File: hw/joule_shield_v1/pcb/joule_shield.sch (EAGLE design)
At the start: 80 parts, among them J4 USB_AUSB_A_SMT_RA, J5 JST-ZH5JST_ZH_SMT_VERT, J6 INTEL_JOULE_J6, J7 INTEL_JOULE_J7, U1 BQ25892PWQFN-24, U2 FAN8623WLCSP16, U3 TPS63201PVSON-14, U4 TLV62084PWSON-8, U5 TPS2553PWSON-6, U6 TPS2553PWSON-6, U7 SINGLE-BIT_BUS_TRANSCEIVER, U8 SINGLE-BIT_BUS_TRANSCEIVER

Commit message: Schematic for RTC battery.
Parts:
- added D3: ESD_DIODEM1005, joule_shield:ESD_DIODEM1005
- added JRTC: BK-916BK-916, joule_shield:BK-916BK-916
- added R25: 1k, mf_passives:RESISTOR_0603
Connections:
- new net N$30: D3.P$2, JRTC.VBAT, R25.P$1
- new net VRTC: R25.P$2
- net GND: now also D3.P$1, JRTC.GND
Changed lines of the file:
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@@
 <part name="U$33" library="joule_shield" deviceset="V5P0V_USBB" device=""/>
 <part name="GND34" library="supply1" deviceset="GND" device=""/>
+<part name="JRTC" library="joule_shield" deviceset="BK-916" device="BK-916"/>
+<part name="GND35" library="supply1" deviceset="GND" device=""/>
+<part name="R25" library="mf_passives" deviceset="RESISTOR" device="_0603" value="1k">
+<attribute name="MPN" value="MF-RES-0603-1K"/>
+</part>
+<part name="U$37" library="joule_shield" deviceset="VRTC" device=""/>
+<part name="GND36" library="supply1" deviceset="GND" device=""/>
+<part name="D3" library="joule_shield" deviceset="ESD_DIODE" device="M1005">
+<attribute name="DPN" value="490-13209-1-ND"/>
+<attribute name="MPN" value="LXES15AAA1-133"/>
+</part>
 </parts>
 <sheets>
@@
 </segment>
 </net>
+</nets>
+</sheet>
+<sheet>
+<plain>
+</plain>
+<instances>
+<instance part="JRTC" gate="G$1" x="17.78" y="45.72"/>
+<instance part="GND35" gate="1" x="43.18" y="30.48"/>
+<instance part="R25" gate="G$1" x="60.96" y="50.8" rot="R90"/>
+<instance part="U$37" gate="G$1" x="78.74" y="58.42"/>
+<instance part="GND36" gate="1" x="55.88" y="22.86"/>
+<instance part="D3" gate="G$1" x="55.88" y="38.1" rot="R90">
+<attribute name="DPN" x="55.88" y="38.1" size="1.778" layer="96" rot="R90" display="off"/>
+<attribute name="MPN" x="55.88" y="38.1" size="1.778" layer="96" rot="R90" display="off"/>
+</instance>
+</instances>
+<busses>
+</busses>
+<nets>
+<net name="GND" class="0">
+<segment>
+<pinref part="JRTC" gate="G$1" pin="GND"/>
+<wire x1="35.56" y1="38.1" x2="43.18" y2="38.1" width="0.1524" layer="91"/>
+<pinref part="GND35" gate="1" pin="GND"/>
+<wire x1="43.18" y1="38.1" x2="43.18" y2="33.02" width="0.1524" layer="91"/>
+</segment>
+<segment>
+<pinref part="D3" gate="G$1" pin="P$1"/>
+<pinref part="GND36" gate="1" pin="GND"/>
+<wire x1="55.88" y1="27.94" x2="55.88" y2="25.4" width="0.1524" layer="91"/>
+</segment>
+</net>
+<net name="VRTC" class="0">
+<segment>
+<pinref part="R25" gate="G$1" pin="P$2"/>
+<pinref part="U$37" gate="G$1" pin="VRTC"/>
+<wire x1="66.04" y1="50.8" x2="78.74" y2="50.8" width="0.1524" layer="91"/>
+<wire x1="78.74" y1="50.8" x2="78.74" y2="58.42" width="0.1524" layer="91"/>
+</segment>
+</net>
+<net name="N$30" class="0">
+<segment>
+<pinref part="R25" gate="G$1" pin="P$1"/>
+<pinref part="JRTC" gate="G$1" pin="VBAT"/>
+<wire x1="55.88" y1="50.8" x2="35.56" y2="50.8" width="0.1524" layer="91"/>
+<pinref part="D3" gate="G$1" pin="P$2"/>
+<wire x1="55.88" y1="48.26" x2="55.88" y2="50.8" width="0.1524" layer="91"/>
+<junction x="55.88" y="50.8"/>
+</segment>
+</net>

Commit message: Add part numbers for all the major ICs and schematic for SD card.
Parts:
- added C33, C34, C36: 0.1uF, mf_passives:CAPACITOR_NP_0603
- added C35: 10uF, mf_passives:CAPACITOR_NP_0603
- added FB1, FB2: FERRITE_BEAD, joule_shield:FERRITE_BEAD
- added R26: 100k, mf_passives:RESISTOR_0603
- added U$40: DM3ATDM3AT, joule_shield:DM3ATDM3AT
- added U9: TXS0206-29, joule_shield:TXS0206-29
- J6, J7: DPN (none) -> H11615CT-ND; MF (none) -> Hirose Electric Co Ltd; MPN (none) -> DF40C-100DS-0.4V(51)
- JD1, JD2: DPN (none) -> 455-2262-1-ND; MF (none) -> JST Sales America Inc.; MPN (none) -> S4B-XH-SM4-TB(LF)(SN)
- JRTC: DPN (none) -> BK-916-CT-ND; MF (none) -> MPD (Memory Protection Devices); MPN (none) -> BK-916-TR
- U1: DPN (none) -> 296-41131-1-ND; MF (none) -> Texas Instruments; MPN (none) -> BQ25892RTWT
- U3: DPN (none) -> 296-27259-1-ND; MF (none) -> Texas Instruments; MPN (none) -> TPS63021DSJR
- U4: MF (none) -> Texas Instruments; MOUSER (none) -> 595-TLV62084DSGR; MPN (none) -> TLV62084DSGR
- U5, U6: DPN (none) -> 296-23999-1-ND; MF (none) -> Texas Instruments; MPN (none) -> TPS2553DRVT
- U7, U8: DPN (none) -> 296-16843-1-ND; MF (none) -> Texas Instruments; MPN (none) -> SN74LVC1T45DBVR
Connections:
- new net N$35: C36.P$1, U$40.VDD, U9.VCCB
- new net N$37: C34.P$1, C35.P$1, FB2.P$1, U9.VBATT
- new net N$38: C33.P$1, FB1.P$2, U9.VCCA
- new net N$40: U$40.DAT0, U9.DAT0B
- new net N$41: U$40.DAT1, U9.DAT1B
- new net N$42: U$40.DAT2, U9.DAT2B
- new net N$43: U$40.CD/DAT3, U9.DAT3B
- new net N$44: U$40.CMD, U9.CMDB
- new net N$45: U$40.CLK, U9.CLKB
- new net SDCARD_CD: J6.SDCARD_CD_N, U$40.CDA, U9.WP/CD
- new net SDCARD_CLK: J6.SDCARD_CLK, U9.CLKA
- new net SDCARD_CLK_FB: J6.SDCARD_LVL_CLK_FB, U9.CLK-F
- new net SDCARD_CMD: J6.SDCARD_CMD, U9.CMDA
- new net SDCARD_D0: J6.SDCARD_D0, U9.DAT0A
- new net SDCARD_D1: J6.SDCARD_D1, U9.DAT1A
- new net SDCARD_D2: J6.SDCARD_D2, U9.DAT2A
- new net SDCARD_D3: J6.SDCARD_D3, U9.DAT3A
- new net SDCARD_PWR_DOWN_N: J6.SDCARD_PWR_DOWN_N, R26.P$1, U9.EN
- net GND: now also C33.P$2, C34.P$2, C35.P$2, C36.P$2, R26.P$2, U$40.CDB, U$40.GND, U$40.VSS, U9.GND
- net V1P8V: now also FB1.P$1
- net V3P3V: now also FB2.P$2

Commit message: Schematic for Fan, BIOS USB-serial, and LEDs.
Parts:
- added C37, C38, C39, C40: 0.1uF, mf_passives:CAPACITOR_NP_0603
- added D10, D11: MF-LED-0603-GREEN, mf_leds:LED_SINGLE-0603-GREEN
- added D4, D5, D6, D7: ESD_DIODEM1005, joule_shield:ESD_DIODEM1005
- added D8, D9: MF-LED-0603-RED, mf_leds:LED_SINGLE-0603-RED
- added FB3: FERRITE_BEAD, joule_shield:FERRITE_BEAD
- added J1: MF-CON-MICROUSB-RIGHT, mf_connectors:USB_MICRO_RIGHT
- added R27: 10k, mf_passives:RESISTOR_0603
- added R28, R29: 27, mf_passives:RESISTOR_0603
- added R30: 0, mf_passives:RESISTOR_0603
- added R31: 100, mf_passives:RESISTOR_0603
- added R32: 100k, mf_passives:RESISTOR_0603
- added R33, R34, R35, R36: 1k, mf_passives:RESISTOR_0603
- added R37, R38, R39, R40: 470, mf_passives:RESISTOR_0603
- added SW1, SW2, SW3: MF-SW-TACT-6MM, mf_switches:TACT_6MM
- added U$41: AMP_MINI_FAN, joule_shield:AMP_MINI_FAN
- added U10: FT231XQFN-20, joule_shield:FT231XQFN-20
- added U11, U12, U13, U14: MF-DSC-SOT233-MMBT3904, mf_discrete_semiconductor:NPN_BJTMMBT3904_SOT-23-3
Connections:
- new net BTN_N: D7.P$2, J6.GPIO_17, SW3.P$2
- new net ISH_GPIO_0: J6.ISH_GPIO_0, R33.P$1
- new net ISH_GPIO_1: J6.ISH_GPIO_1, R34.P$1
- new net ISH_GPIO_2: J6.ISH_GPIO_2, R35.P$1
- new net ISH_GPIO_3: J6.ISH_GPIO_3, R36.P$1
- new net N$36: R27.P$2, U$41.2
- new net N$39: R28.P$2, U10.USBDM
- new net N$46: D4.P$2, FB3.P$1, J1.5V
- new net N$47: R29.P$2, U10.USBDP
- new net N$48: J1.D+, R29.P$1
- new net N$49: C38.P$1, FB3.P$2, U10.VCC
- new net N$50: J1.D-, R28.P$1
- new net N$51: R30.P$2, U1./QON
- new net N$52: R31.P$2, SW2.P$3
- new net N$53: C40.P$1, U10.3V3OUT
- new net N$54: R32.P$2, SW3.P$1
- new net N$55: D11.ANODE, R40.P$2
- new net N$56: D10.ANODE, R39.P$2
- new net N$57: D9.ANODE, R38.P$2
- new net N$58: D8.ANODE, R37.P$2
- new net N$59: D8.CATHODE, U11.COLLECTOR
- new net N$60: D9.CATHODE, U12.COLLECTOR
- new net N$61: D10.CATHODE, U13.COLLECTOR
- new net N$62: D11.CATHODE, U14.COLLECTOR
- new net N$63: R33.P$2, U11.BASE
- new net N$64: R34.P$2, U12.BASE
- new net N$65: R35.P$2, U13.BASE
- new net N$66: R36.P$2, U14.BASE
- new net PMIC_PWRBTN_N: D5.P$2, R30.P$1, SW1.P$2
- new net UART2_CTS: J6.UART2_CTS, U10.RTS/
- new net UART2_RTS: J6.UART2_RTS, U10.CTS/
- new net UART2_RX: J6.UART2_RXD, U10.TXD
- new net UART2_TX: D6.P$2, J6.UART2_TXD, SW2.P$2, U10.RXD
- net GND: now also C37.P$2, C38.P$2, C39.P$2, C40.P$2, D4.P$1, D5.P$1, D6.P$1, D7.P$1, J1.GND, J1.SLD, SW1.P$3, SW3.P$3, U$41.3, U$41.SHLD, U10.AGND, U10.GND, U11.EMITTER, U12.EMITTER, U13.EMITTER, U14.EMITTER
- net V1P8V: now also C39.P$1, U10.VCCIO
- net V3P3V: now also R27.P$1
- net V5P0V: now also C37.P$1, R37.P$1, R38.P$1, R39.P$1, R40.P$1, U$41.1
- net VDD1: now also R31.P$1, R32.P$1
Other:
- note added: "Boot from DNX"
- note added: "Power Button"

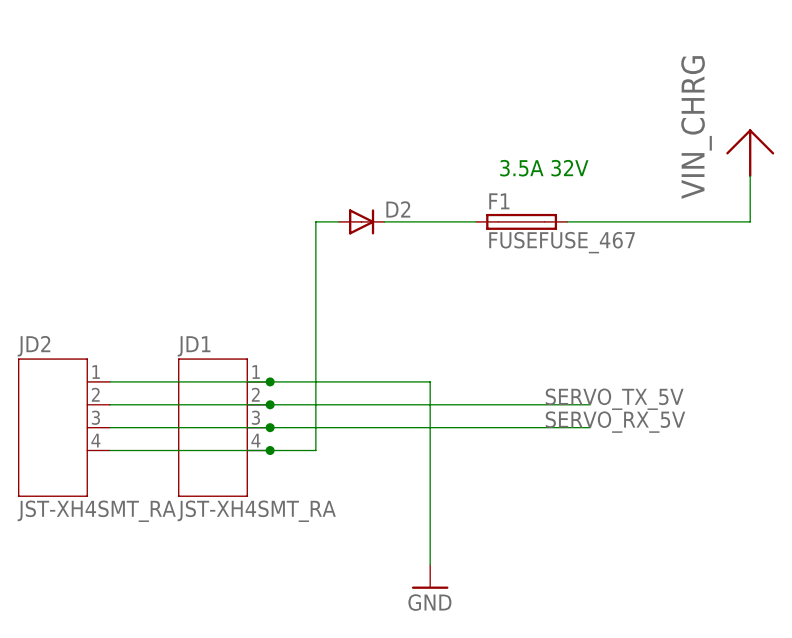
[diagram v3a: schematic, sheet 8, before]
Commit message: joule shield: Begin rough layout.
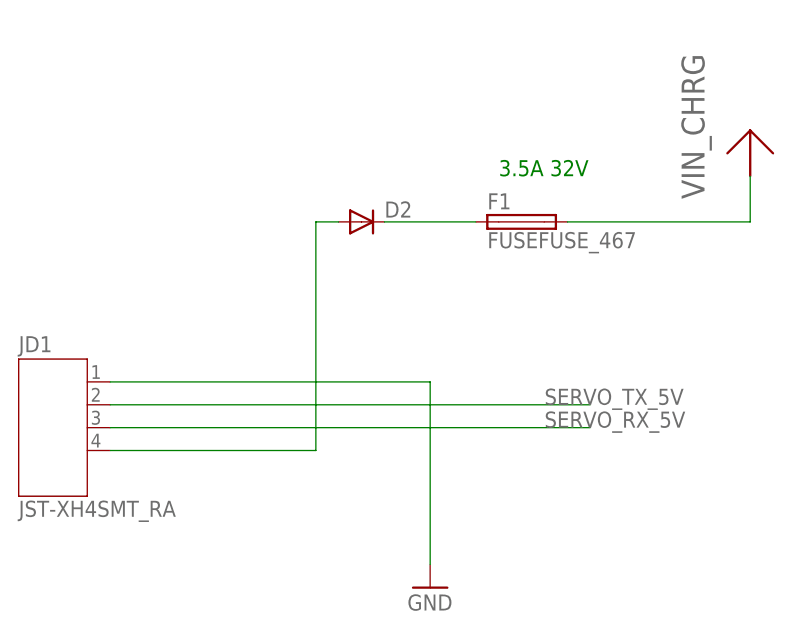
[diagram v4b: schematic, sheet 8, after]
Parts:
- removed JD2: JST-XH4SMT_RA, joule_shield:JST-XH4SMT_RA
- added U$48, U$49, U$50, U$51: SMTSOSMTSO-M1.6, joule_shield:SMTSOSMTSO-M1.6
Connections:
- net GND: no longer JD2.1
- net N$28: no longer JD2.4
- net SERVO_RX_5V: no longer JD2.3
- net SERVO_TX_5V: no longer JD2.2
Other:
- moved on the sheet: JD1
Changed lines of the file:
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@@
 </part>
 <part name="U$26" library="joule_shield" deviceset="V1P8V" device=""/>
-<part name="JD1" library="joule_shield" deviceset="JST-XH4" device="SMT_RA">
-<attribute name="DPN" value="455-2262-1-ND"/>
-<attribute name="MF" value="JST Sales America Inc."/>
-<attribute name="MPN" value="S4B-XH-SM4-TB(LF)(SN)"/>
-</part>
 <part name="GND26" library="supply1" deviceset="GND" device=""/>
 <part name="U$28" library="joule_shield" deviceset="VIN_CHRG" device=""/>
-<part name="JD2" library="joule_shield" deviceset="JST-XH4" device="SMT_RA">
+<part name="JD1" library="joule_shield" deviceset="JST-XH4" device="SMT_RA">
 <attribute name="DPN" value="455-2262-1-ND"/>
 <attribute name="MF" value="JST Sales America Inc."/>
@@
 </part>
 <part name="U$47" library="joule_shield" deviceset="V5P0V" device=""/>
+<part name="U$48" library="joule_shield" deviceset="SMTSO" device="SMTSO-M1.6"/>
+<part name="U$49" library="joule_shield" deviceset="SMTSO" device="SMTSO-M1.6"/>
+<part name="U$50" library="joule_shield" deviceset="SMTSO" device="SMTSO-M1.6"/>
+<part name="U$51" library="joule_shield" deviceset="SMTSO" device="SMTSO-M1.6"/>
 </parts>
 <sheets>
@@
 <instance part="U$33" gate="G$1" x="279.4" y="93.98"/>
 <instance part="GND34" gate="1" x="287.02" y="60.96"/>
+<instance part="U$48" gate="G$1" x="-25.4" y="-22.86"/>
+<instance part="U$49" gate="G$1" x="-7.62" y="-22.86"/>
+<instance part="U$50" gate="G$1" x="10.16" y="-22.86"/>
+<instance part="U$51" gate="G$1" x="27.94" y="-22.86"/>
 </instances>
 <busses>
@@
 </plain>
 <instances>
-<instance part="JD1" gate="G$1" x="35.56" y="83.82">
-<attribute name="DPN" x="35.56" y="83.82" size="1.778" layer="96" display="off"/>
-<attribute name="MF" x="35.56" y="83.82" size="1.778" layer="96" display="off"/>
-<attribute name="MPN" x="35.56" y="83.82" size="1.778" layer="96" display="off"/>
-</instance>
 <instance part="GND26" gate="1" x="60.96" y="66.04"/>
 <instance part="U$28" gate="G$1" x="96.52" y="111.76"/>
-<instance part="JD2" gate="G$1" x="17.78" y="83.82">
+<instance part="JD1" gate="G$1" x="17.78" y="83.82">
 <attribute name="DPN" x="17.78" y="83.82" size="1.778" layer="96" display="off"/>
 <attribute name="MF" x="17.78" y="83.82" size="1.778" layer="96" display="off"/>
@@
 <wire x1="60.96" y1="68.58" x2="60.96" y2="88.9" width="0.1524" layer="91"/>
 <pinref part="JD1" gate="G$1" pin="1"/>
-<wire x1="60.96" y1="88.9" x2="43.18" y2="88.9" width="0.1524" layer="91"/>
-<pinref part="JD2" gate="G$1" pin="1"/>
-<wire x1="25.4" y1="88.9" x2="43.18" y2="88.9" width="0.1524" layer="91"/>
-<junction x="43.18" y="88.9"/>
+<wire x1="25.4" y1="88.9" x2="60.96" y2="88.9" width="0.1524" layer="91"/>
 </segment>
 </net>
 <net name="SERVO_TX_5V" class="0">
 <segment>
+<wire x1="25.4" y1="86.36" x2="78.74" y2="86.36" width="0.1524" layer="91"/>
+<label x="73.66" y="86.36" size="1.778" layer="95"/>
 <pinref part="JD1" gate="G$1" pin="2"/>
-<wire x1="43.18" y1="86.36" x2="78.74" y2="86.36" width="0.1524" layer="91"/>
-<label x="73.66" y="86.36" size="1.778" layer="95"/>
-<pinref part="JD2" gate="G$1" pin="2"/>
-<wire x1="43.18" y1="86.36" x2="25.4" y2="86.36" width="0.1524" layer="91"/>
-<junction x="43.18" y="86.36"/>
 </segment>
 </net>
 <net name="SERVO_RX_5V" class="0">
 <segment>
+<wire x1="25.4" y1="83.82" x2="78.74" y2="83.82" width="0.1524" layer="91"/>
+<label x="73.66" y="83.82" size="1.778" layer="95"/>
 <pinref part="JD1" gate="G$1" pin="3"/>
-<wire x1="43.18" y1="83.82" x2="78.74" y2="83.82" width="0.1524" layer="91"/>
-<label x="73.66" y="83.82" size="1.778" layer="95"/>
-<pinref part="JD2" gate="G$1" pin="3"/>
-<wire x1="25.4" y1="83.82" x2="43.18" y2="83.82" width="0.1524" layer="91"/>
-<junction x="43.18" y="83.82"/>
 </segment>
 </net>
@@
 <segment>
 <pinref part="JD1" gate="G$1" pin="4"/>
-<wire x1="43.18" y1="81.28" x2="48.26" y2="81.28" width="0.1524" layer="91"/>
-<pinref part="JD2" gate="G$1" pin="4"/>
-<wire x1="25.4" y1="81.28" x2="43.18" y2="81.28" width="0.1524" layer="91"/>
-<junction x="43.18" y="81.28"/>
+<wire x1="25.4" y1="81.28" x2="48.26" y2="81.28" width="0.1524" layer="91"/>
 <pinref part="D2" gate="G$1" pin="A"/>
 <wire x1="50.8" y1="106.68" x2="48.26" y2="106.68" width="0.1524" layer="91"/>

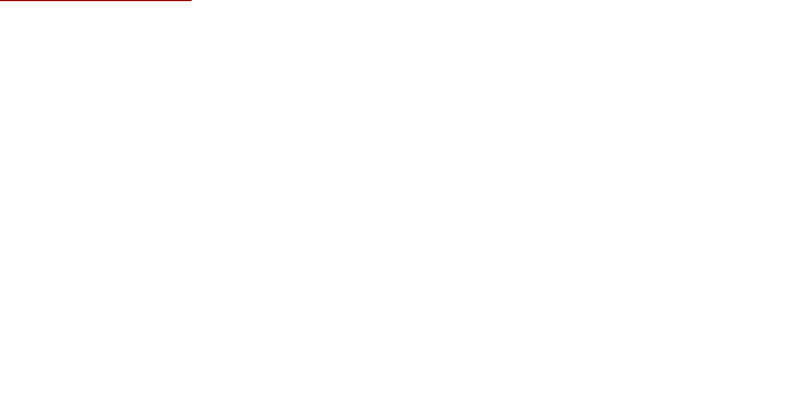
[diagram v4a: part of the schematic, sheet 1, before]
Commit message: Work on Joule connectors and mounting holes.
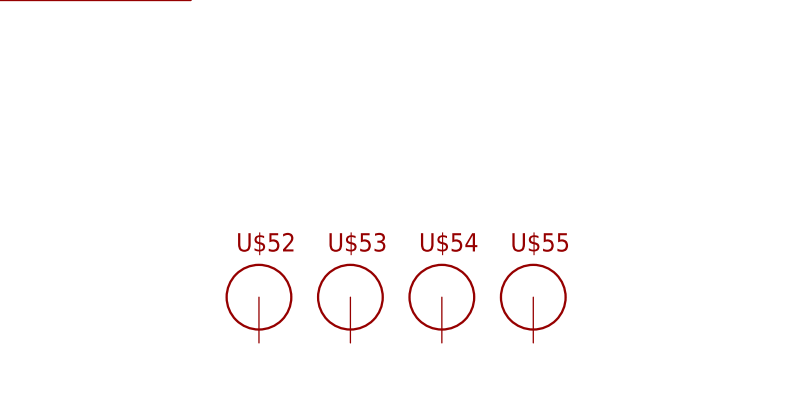
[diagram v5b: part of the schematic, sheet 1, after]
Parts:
- added U$52, U$53, U$54, U$55: M2.5MOUNT, joule_shield:M2.5MOUNT
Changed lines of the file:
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@@
 <part name="U$50" library="joule_shield" deviceset="SMTSO" device="SMTSO-M1.6"/>
 <part name="U$51" library="joule_shield" deviceset="SMTSO" device="SMTSO-M1.6"/>
+<part name="U$52" library="joule_shield" deviceset="M2.5MOUNT" device=""/>
+<part name="U$53" library="joule_shield" deviceset="M2.5MOUNT" device=""/>
+<part name="U$54" library="joule_shield" deviceset="M2.5MOUNT" device=""/>
+<part name="U$55" library="joule_shield" deviceset="M2.5MOUNT" device=""/>
 </parts>
 <sheets>
@@
 <instance part="U$50" gate="G$1" x="10.16" y="-22.86"/>
 <instance part="U$51" gate="G$1" x="27.94" y="-22.86"/>
+<instance part="U$52" gate="G$1" x="83.82" y="-17.78"/>
+<instance part="U$53" gate="G$1" x="93.98" y="-17.78"/>
+<instance part="U$54" gate="G$1" x="104.14" y="-17.78"/>
+<instance part="U$55" gate="G$1" x="114.3" y="-17.78"/>
 </instances>
 <busses>

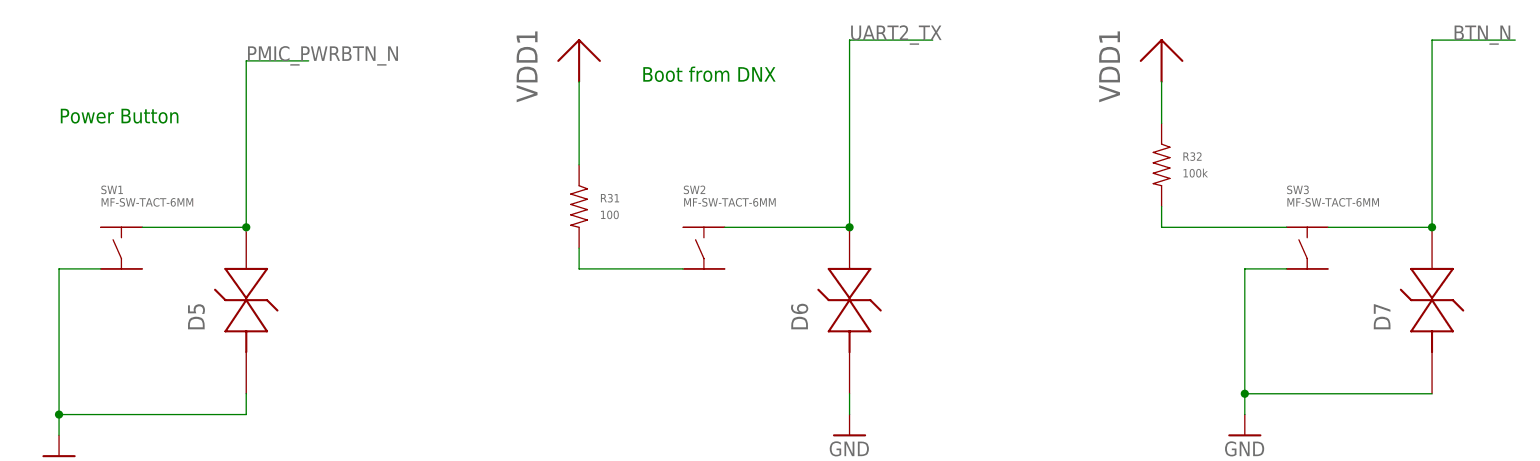
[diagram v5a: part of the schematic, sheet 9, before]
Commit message: Change switches to 4.2mm ones, and continue with draft placement.
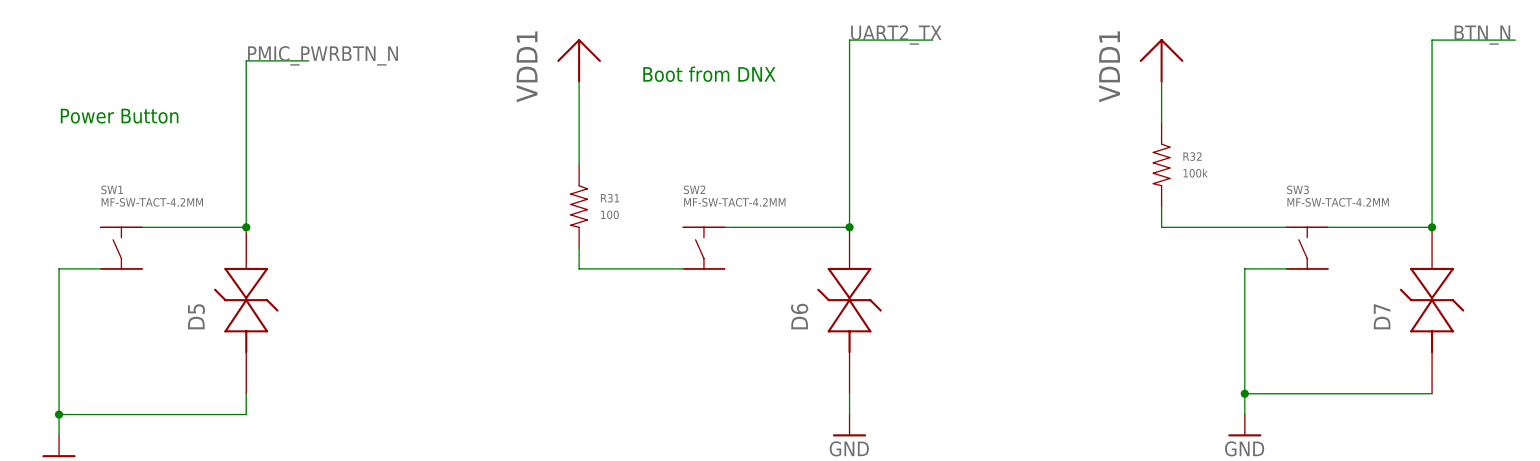
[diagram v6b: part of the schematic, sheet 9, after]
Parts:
- SW1, SW2, SW3: value MF-SW-TACT-6MM -> MF-SW-TACT-4.2MM; device mf_switches:TACT_6MM -> mf_switches:TACT_4.2MM
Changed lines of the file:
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@@
 <attribute name="MPN" value="MF-RES-0603-27"/>
 </part>
-<part name="SW1" library="mf_switches" deviceset="TACT" device="_6MM" value="MF-SW-TACT-6MM"/>
-<part name="SW2" library="mf_switches" deviceset="TACT" device="_6MM" value="MF-SW-TACT-6MM"/>
-<part name="SW3" library="mf_switches" deviceset="TACT" device="_6MM" value="MF-SW-TACT-6MM"/>
+<part name="SW1" library="mf_switches" deviceset="TACT" device="_4.2MM" value="MF-SW-TACT-4.2MM"/>
+<part name="SW2" library="mf_switches" deviceset="TACT" device="_4.2MM" value="MF-SW-TACT-4.2MM"/>
+<part name="SW3" library="mf_switches" deviceset="TACT" device="_4.2MM" value="MF-SW-TACT-4.2MM"/>
 <part name="GND48" library="supply1" deviceset="GND" device=""/>
 <part name="D5" library="joule_shield" deviceset="ESD_DIODE" device="M1005">
